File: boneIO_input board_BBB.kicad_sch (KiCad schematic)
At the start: 395 parts, among them J1 Screw_Terminal_01x08, J10 Screw_Terminal_01x04, J11 BeagleBone_Black_Header, J12 BeagleBone_Black_Header, J13 Conn_02x04_Odd_Even, J14 Screw_Terminal_01x08, J2 Screw_Terminal_01x08, J3 Screw_Terminal_01x08, J4 EXT_PSU, J5 Screw_Terminal_01x08, J6 Screw_Terminal_01x08, J7 Screw_Terminal_01x08, J8 Screw_Terminal_01x08, J9 Screw_Terminal_01x08, Q1 BSS84, SW1 SW_Push, SW2 SW_DIP_x04, U1 XL1509-5, U10 EL357N, U11 EL357N, U12 EL357N, U13 EL357N, U14 EL357N, U15 EL357N, U16 EL357N, U17 EL357N, U18 EL357N, U19 RT9013-33GB, U2 HLK-5D2405, U20 EL357N, U21 EL357N, U22 EL357N, U23 EL357N, U24 EL357N, U25 EL357N, U26 EL357N, U27 EL357N, U28 2N7002DW/BSS138PS, U29 EL357N, U3 EL357N, U30 EL357N, U31 EL357N, U32 EL357N, U33 EL357N, U34 EL357N, U35 EL357N, U36 EL357N, U37 DS1307Z+, U38 EL357N, U39 EL357N, U4 EL357N, U40 EL357N, U41 EL357N, U42 EL357N, U43 EL357N, U44 EL357N, U45 EL357N, U46 EL357N, U47 EL357N, U48 EL357N, U49 EL357N, U5 EL357N, U50 EL357N, U51 EL357N, U52 EL357N, U53 EL357N, U54 EL357N, U55 SN65HVD230, U56 RS485, U57 PCA9515, U58 PCA9515, U59 DS2482S-100+, U6 EL357N, U60 INA219AxD, U7 EL357N, U8 EL357N, U9 EL357N, Y1 32,788 MHz

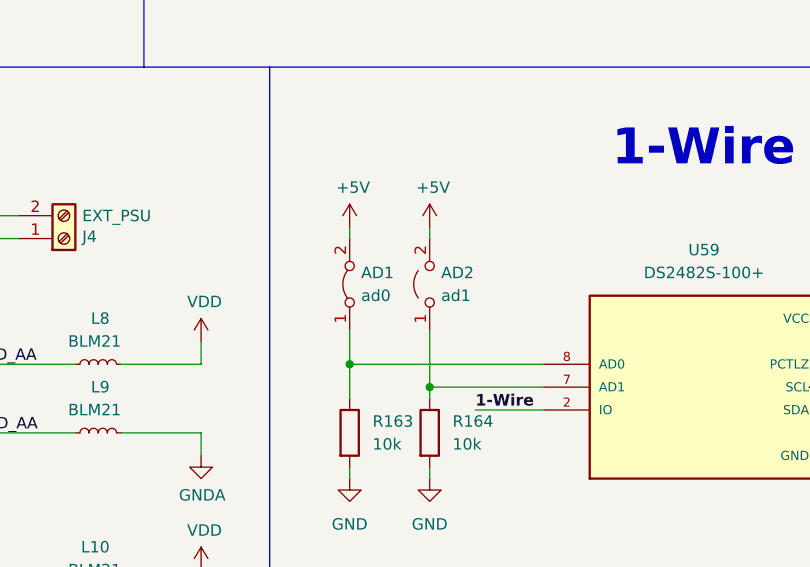
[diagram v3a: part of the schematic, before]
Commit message: input_board_v0.4
final version
descriptions added
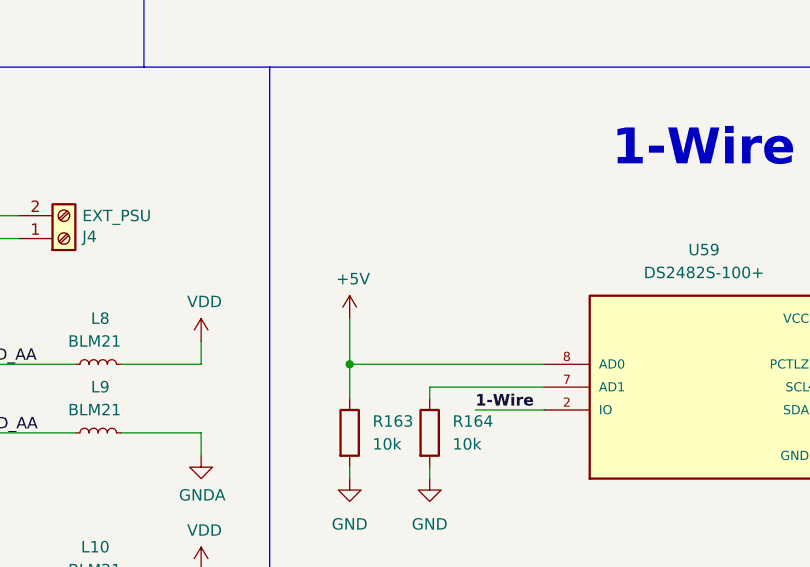
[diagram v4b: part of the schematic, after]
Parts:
- removed AD1: ad0, Jumper:SolderJumper-2_P1.3mm_Bridged2Bar_RoundedPad1.0x1.5mm, symbol Jumper:Jumper_2_Bridged
- removed AD2: ad1, Jumper:SolderJumper-2_P1.3mm_Open_RoundedPad1.0x1.5mm, symbol Jumper:Jumper_2_Open
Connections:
- net +5V: now also R163.1, U59.8 (AD0)
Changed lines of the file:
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@@
   (junction (at 402.59 459.74) (diameter 0) (color 0 0 0 0)
   )
-  (junction (at 652.78 410.21) (diameter 0) (color 0 0 0 0)
-  )
   (junction (at 170.18 229.87) (diameter 0) (color 0 0 0 0)
   )
@@
     (stroke (width 0) (type default) (color 0 0 0 0))
   )
-  (wire (pts (xy 652.78 392.43) (xy 652.78 393.7))
-    (stroke (width 0) (type default) (color 0 0 0 0))
-  )
   (wire (pts (xy 95.25 179.07) (xy 106.68 179.07))
     (stroke (width 0) (type default) (color 0 0 0 0))
@@
     (stroke (width 0) (type default) (color 0 0 0 0))
   )
-  (wire (pts (xy 643.89 403.86) (xy 643.89 407.67))
+  (wire (pts (xy 643.89 402.59) (xy 643.89 407.67))
     (stroke (width 0) (type default) (color 0 0 0 0))
   )
@@
     (stroke (width 0) (type default) (color 0 0 0 0))
   )
-  (wire (pts (xy 643.89 392.43) (xy 643.89 393.7))
-    (stroke (width 0) (type default) (color 0 0 0 0))
-  )
   (wire (pts (xy 567.69 347.98) (xy 570.23 347.98))
     (stroke (width 0) (type default) (color 0 0 0 0))
@@
     (stroke (width 0) (type default) (color 0 0 0 0))
   )
-  (wire (pts (xy 652.78 403.86) (xy 652.78 410.21))
-    (stroke (width 0) (type default) (color 0 0 0 0))
-  )
   (wire (pts (xy 247.65 312.42) (xy 254 312.42))
     (stroke (width 0) (type default) (color 0 0 0 0))
@@
     (pin "1")
   )
-  (symbol (lib_id "Jumper:Jumper_2_Bridged") (at 643.89 398.78 90) (unit 1)
-    (in_bom yes) (on_board yes) (fields_autoplaced)
-    (property "Reference" "AD1" (id 0) (at 645.16 397.5099 90)
-      (effects (font (size 1.27 1.27)) (justify right))
-    )
-    (property "Value" "ad0" (id 1) (at 645.16 400.0499 90)
-      (effects (font (size 1.27 1.27)) (justify right))
-    )
-    (property "Footprint" "Jumper:SolderJumper-2_P1.3mm_Bridged2Bar_RoundedPad1.0x1.5mm" (id 2) (at 643.89 398.78 0)
-      (effects (font (size 1.27 1.27)) hide)
-    )
-    (property "Datasheet" "~" (id 3) (at 643.89 398.78 0)
-      (effects (font (size 1.27 1.27)) hide)
-    )
-    (pin "1")
-    (pin "2")
-  )
   (symbol (lib_id "Device:R") (at 486.41 373.38 180) (unit 1)
     (in_bom yes) (on_board yes)
@@
     (pin "2")
   )
-  (symbol (lib_id "power:+5V") (at 652.78 392.43 0) (unit 1)
-    (in_bom yes) (on_board yes)
-    (property "Reference" "#PWR0333" (id 0) (at 652.78 396.24 0)
-      (effects (font (size 1.27 1.27)) hide)
-    )
-    (property "Value" "+5V" (id 1) (at 653.161 388.0358 0))
-    (property "Footprint" "" (id 2) (at 652.78 392.43 0)
-      (effects (font (size 1.27 1.27)) hide)
-    )
-    (property "Datasheet" "" (id 3) (at 652.78 392.43 0)
-      (effects (font (size 1.27 1.27)) hide)
-    )
-    (pin "1")
-  )
   (symbol (lib_id "Device:L_Small") (at 537.21 419.1 270) (unit 1)
     (in_bom yes) (on_board yes)
@@
     (pin "1")
   )
-  (symbol (lib_id "power:+5V") (at 643.89 392.43 0) (unit 1)
+  (symbol (lib_id "power:+5V") (at 643.89 402.59 0) (unit 1)
     (in_bom yes) (on_board yes)
-    (property "Reference" "#PWR0326" (id 0) (at 643.89 396.24 0)
+    (property "Reference" "#PWR0326" (id 0) (at 643.89 406.4 0)
       (effects (font (size 1.27 1.27)) hide)
     )
-    (property "Value" "+5V" (id 1) (at 644.271 388.0358 0))
-    (property "Footprint" "" (id 2) (at 643.89 392.43 0)
+    (property "Value" "+5V" (id 1) (at 644.271 398.1958 0))
+    (property "Footprint" "" (id 2) (at 643.89 402.59 0)
       (effects (font (size 1.27 1.27)) hide)
     )
-    (property "Datasheet" "" (id 3) (at 643.89 392.43 0)
+    (property "Datasheet" "" (id 3) (at 643.89 402.59 0)
       (effects (font (size 1.27 1.27)) hide)
     )
@@
     (pin "1")
   )
-  (symbol (lib_id "Jumper:Jumper_2_Open") (at 652.78 398.78 90) (unit 1)
-    (in_bom yes) (on_board yes) (fields_autoplaced)
-    (property "Reference" "AD2" (id 0) (at 654.05 397.5099 90)
-      (effects (font (size 1.27 1.27)) (justify right))
-    )
-    (property "Value" "ad1" (id 1) (at 654.05 400.0499 90)
-      (effects (font (size 1.27 1.27)) (justify right))
-    )
-    (property "Footprint" "Jumper:SolderJumper-2_P1.3mm_Open_RoundedPad1.0x1.5mm" (id 2) (at 652.78 398.78 0)
-      (effects (font (size 1.27 1.27)) hide)
-    )
-    (property "Datasheet" "~" (id 3) (at 652.78 398.78 0)
-      (effects (font (size 1.27 1.27)) hide)
-    )
-    (pin "1")
-    (pin "2")
-  )
   (symbol (lib_id "Device:LED_ALT") (at 486.41 266.7 90) (unit 1)
     (in_bom yes) (on_board yes)
@@
       (reference "#PWR0332") (unit 1) (value "GND") (footprint "")
     )
-    (path "/747e0037-5432-4d12-a50b-f417311ff954"
-      (reference "#PWR0333") (unit 1) (value "+5V") (footprint "")
-    )
     (path "/93c6fa48-78e3-448c-b7a0-b783a173c002"
       (reference "#PWR0334") (unit 1) (value "GND") (footprint "")
@@
       (reference "#PWR0370") (unit 1) (value "Earth") (footprint "")
     )
-    (path "/16d9ee91-9f7e-4305-88b4-ae4dabd60b80"
-      (reference "AD1") (unit 1) (value "ad0") (footprint "Jumper:SolderJumper-2_P1.3mm_Bridged2Bar_RoundedPad1.0x1.5mm")
-    )
-    (path "/a311dad9-240d-4934-809a-861307cc6006"
-      (reference "AD2") (unit 1) (value "ad1") (footprint "Jumper:SolderJumper-2_P1.3mm_Open_RoundedPad1.0x1.5mm")
-    )
     (path "/00000000-0000-0000-0000-000062d1d94e"

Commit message: input_board_v7.1
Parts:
- removed BT1: Battery, Battery:Battery_Panasonic_CR1220-VCN_Vertical_CircularHoles, symbol Device:Battery
- removed C20, C22: 1uF, Capacitor_SMD:C_0805_2012Metric, symbol Device:C
- removed C21: 460p, Capacitor_SMD:C_0603_1608Metric, symbol Device:C
- removed C40, C59, C61: 100n, Capacitor_SMD:C_0603_1608Metric, symbol Device:C
- removed D12, D15, D16, D17, D18, D19, D2, D22, D23, D24, D25, D26, D27, D28, D29, D3, D30, D31, D32, D33, D34, D35, D36, D37, D38, D39, D4, D40, D41, D42, D43, D44, D45, D46, D47, D48, D49, D5, D50, D53, D54, D55, D56, D6, D9: LED, LED_SMD:LED_0603_1608Metric, symbol Device:LED_ALT
- removed D51, D52: B5819W, Diode_SMD:D_SOD-123, symbol Device:D_ALT
- removed D57, D58: LED_GREEN, Capacitor_SMD:C_0805_2012Metric, symbol Device:LED
- removed D60: 5V6, Diode_SMD:D_MiniMELF, symbol Device:D_Zener_ALT
- removed D61: PESD5V0S2BT, Package_TO_SOT_SMD:SOT-23, symbol Diode:BAT54A
- removed J4: EXT_PSU, Connector_Phoenix_MSTB:PhoenixContact_MSTBA_2,5_2-G_1x02_P5.00mm_Horizontal, symbol Connector:Screw_Terminal_01x02
- removed L10, L11, L2, L3, L8, L9: BLM21, Inductor_SMD:L_0805_2012Metric, symbol Device:L_Small
- removed L5, L6, L7: BLM21_NC, Inductor_SMD:L_0805_2012Metric, symbol Device:L_Small
- removed Q1: BSS84, Package_TO_SOT_SMD:SOT-23, symbol Transistor_FET:BSS84
- removed R106, R130, R131, R146, R159, R51, R78: 680R, Resistor_SMD:R_0603_1608Metric, symbol Device:R
- removed R115: 10k, Resistor_SMD:R_0603_1608Metric, symbol Device:R
- removed R35: 100k, Resistor_SMD:R_0603_1608Metric, symbol Device:R
- removed R89, R90: 4.7k, Resistor_SMD:R_0603_1608Metric, symbol Device:R
- removed U19: RT9013-33GB, Package_TO_SOT_SMD:SOT-23-5, symbol Reference_Voltage:RT9013-33GB
- removed U2: HLK-5D2405, 3D_model:HLK5D2405, symbol Power_Management:HLK-5D2405
- removed U28: 2N7002DW/BSS138PS, Package_TO_SOT_SMD:SOT-363_SC-70-6, symbol Transistor_FET:2N7002DW
- removed U37: DS1307Z+, Package_SO:SOIC-8_3.9x4.9mm_P1.27mm, symbol Timer_RTC:DS1307Z+
- removed U56: RS485, rs485:RS485_moduleTTL, symbol RS485:RS485_module
- removed U57: PCA9515, Package_SO:TSSOP-8_3x3mm_P0.65mm, symbol Interface_Expansion:PCA9515
- removed U58: PCA9515, Package_SO:SO-8_3.9x4.9mm_P1.27mm, symbol Interface_Expansion:PCA9515
- removed U59: DS2482S-100+, Package_SO:SOP-8_3.9x4.9mm_P1.27mm, symbol DS2482S-100_:DS2482S-100+
- removed WIRE1: SPU, Jumper:SolderJumper-2_P1.3mm_Open_RoundedPad1.0x1.5mm, symbol Jumper:Jumper_2_Open
- removed Y1: 32,788 MHz, Crystal:Crystal_C26-LF_D2.1mm_L6.5mm_Horizontal, symbol Device:Crystal
- added C104, C105, C106, C107, C108, C109, C11, C110, C12, C13, C14, C15, C16, C17, C18, C29, C30, C31, C32, C33, C34, C35, C36, C37, C47, C48, C49, C51, C52, C53, C54, C55, C64, C65, C66, C67, C68, C69, C70, C71, C81, C82, C83, C84, C85, C86, C87, C88, C94, C95, C96, C97, C98: 100n, Capacitor_SMD:C_0603_1608Metric, symbol Device:C
- added C28, C38: 10uF, Capacitor_SMD:C_1206_3216Metric, symbol Device:C
- added D1: SMBJ24CA, Diode_SMD:D_SMB, symbol Diode:SM6T18A
- added D10: SMBJ5.0A, Diode_SMD:D_SMB, symbol Diode:SM6T18A
- added D11, D15: SMLVT3V3, Diode_SMD:D_SOD-323_HandSoldering, symbol Diode:B220
- added D12: SM712_SOT23, Package_TO_SOT_SMD:SOT-23, symbol Diode:SM712_SOT23
- added Q1: BC807, Package_TO_SOT_SMD:SOT-23, symbol Transistor_BJT:BC807
- added Q2: BSS138, Package_TO_SOT_SMD:SOT-23, symbol Transistor_FET:BSS138
- added R122, R123, R141, R155, R43, R70, R98: 680R, Resistor_SMD:R_0603_1608Metric, symbol Device:R
- added R162: 1k, Resistor_SMD:R_1206_3216Metric, symbol Device:R
- added R168, R172: 4.7k, Resistor_SMD:R_0603_1608Metric, symbol Device:R
- added R171: 120R, Resistor_SMD:R_0805_2012Metric, symbol ESP32-EVB_Rev_I:R
- added R173, R178, R179, R180: 0k, Resistor_SMD:R_0603_1608Metric, symbol Device:R
- added R176, R177: 1k, Resistor_SMD:R_0603_1608Metric, symbol Device:R
- added RS485_T1: Opened, Jumper:SolderJumper-2_P1.3mm_Open_RoundedPad1.0x1.5mm, symbol ESP32-EVB_Rev_I:SJ
- added U1: ADuM1250, Package_SO:SOIC-8_3.9x4.9mm_P1.27mm, symbol Isolator:ADuM1250
- added U19: AMS1117-3.3, Package_TO_SOT_SMD:SOT-223-3_TabPin2, symbol Regulator_Linear:AMS1117-3.3
- added U56: MAX485E, Package_SO:SOIC-8_3.9x4.9mm_P1.27mm, symbol Interface_UART:MAX485E
- D13, D14, D7, D8: value LED -> LED_RED
- D4: renamed from D11; footprint LED_SMD:LED_0805_2012Metric -> LED_SMD:LED_0603_1608Metric
- D5: renamed from D20; footprint LED_SMD:LED_0805_2012Metric -> LED_SMD:LED_0603_1608Metric
- F1: value Fuse_2A -> Fuse 2A; footprint Fuse:Fuse_2512_6332Metric -> Fuse:Fuse_1812_4532Metric; JLCPCB C136367 -> (none)
- L4: value BLM21_NC -> BLM21PG121SN1D
- R121: renamed from R123; value 1.5k -> 10k
- R160: renamed from R161; value 330R -> 1k
- R161: renamed from R162; value 330R -> 1k
- R163: value 10k -> 1k; footprint Resistor_SMD:R_0603_1608Metric -> Resistor_SMD:R_1206_3216Metric; JLCPCB (none) -> C101062
- R164: value 10k -> 4.7k
- R165, R166: value 10k -> 4.7k; JLCPCB C269704 -> (none)
- R167: value 50R -> 4.7k; JLCPCB (none) -> C269704
- R169: value 4.7k -> 0k; footprint Resistor_SMD:R_0603_1608Metric -> Resistor_SMD:R_0805_2012Metric
- R170: value 0R -> 0k_NC
- R34: renamed from R26; value 330R -> 1k
- R51: renamed from R52; value 330R -> 1k
- RV1: footprint Varistor:RV_Disc_D7mm_W3.5mm_P5mm -> Resistor_THT:R_Axial_DIN0204_L3.6mm_D1.6mm_P5.08mm_Vertical
- SW2: footprint Button_Switch_SMD:SW_DIP_SPSTx04_Slide_Omron_A6S-410x_W8.9mm_P2.54mm -> Button_Switch_THT:SW_DIP_SPSTx04_Piano_10.8x11.72mm_W7.62mm_P2.54mm
- U11, U12, U13, U14, U15, U16, U17, U18, U20, U21, U22, U23, U24, U25, U26, U27, U29, U30, U31, U32, U33, U34, U35, U36, U46, U47, U48, U49, U50, U51, U52, U53, U54: value EL357N -> EL354N
- U2: renamed from U3; value EL357N -> EL354N
- U3: renamed from U4; value EL357N -> EL354N
- U37: renamed from U38; value EL357N -> EL354N
- U38: renamed from U39; value EL357N -> EL354N
- U39: renamed from U40; value EL357N -> EL354N
- U4: renamed from U5; value EL357N -> EL354N
- U40: renamed from U41; value EL357N -> EL354N
- U41: renamed from U42; value EL357N -> EL354N
- U42: renamed from U43; value EL357N -> EL354N
- U43: renamed from U44; value EL357N -> EL354N
- U44: renamed from U45; value EL357N -> EL354N
- U5: renamed from U6; value EL357N -> EL354N
- U6: renamed from U7; value EL357N -> EL354N
- U7: renamed from U8; value EL357N -> EL354N
- U8: renamed from U9; value EL357N -> EL354N
- U9: renamed from U10; value EL357N -> EL354N
- renumbered C2 to C1, C55 to C100, C56 to C101, C57 to C102, C58 to C103, C60 to C111, C62 to C112, C11 to C19, C3 to C2, C12 to C20, C13 to C21, C14 to C22, C15 to C23, C16 to C24, C17 to C25, C18 to C26, C19 to C27, C4 to C3, C23 to C39, C5 to C4, C24 to C40, C25 to C41, C26 to C42, C27 to C43, C28 to C44, C29 to C45, C30 to C46, C6 to C5, C31 to C50, C32 to C56, C33 to C57, C34 to C58, C35 to C59, C7 to C6, C36 to C60, C37 to C61, C38 to C62, C39 to C63, C8 to C7, C41 to C73, C42 to C74, C43 to C75, C44 to C76, C45 to C77, C46 to C78, C47 to C79, C9 to C8, C48 to C80, C49 to C89, C1 to C9, C50 to C90, C51 to C91, C52 to C92, C53 to C93, C54 to C99, D1 to D2, D10 to D3, D21 to D6, D59 to D9, J9 to J10, J10 to J11, J13 to J12, J14 to J13, J5 to J4, J6 to J5, J11 to J6, J12 to J9, L1 to L3, R11 to R10, R107 to R106, R108 to R107, R109 to R108, R110 to R109, R12 to R11, R111 to R110, R112 to R111, R113 to R112, R114 to R113, R116 to R114, R117 to R115, R118 to R116, R119 to R117, R120 to R118, R121 to R119, R13 to R12, R122 to R120, R14 to R13, R132 to R131, R133 to R132, R134 to R133, R135 to R134, R136 to R135, R137 to R136, R138 to R137, R139 to R138, R140 to R139, R15 to R14, R141 to R140, R147 to R146, R148 to R147, R149 to R148, R150 to R149, R16 to R15, R151 to R150, R152 to R151, R153 to R152, R154 to R153, R155 to R154, R160 to R159, R17 to R16, R9 to R17, R168 to R174, R171 to R175, R27 to R26, R28 to R27, R29 to R28, R30 to R29, R31 to R30, R32 to R31, R33 to R32, R34 to R33, R36 to R35, R37 to R36, R38 to R37, R39 to R38, R40 to R39, R41 to R40, R42 to R41, R43 to R42, R53 to R52, R54 to R53, R55 to R54, R56 to R55, R57 to R56, R58 to R57, R59 to R58, R60 to R59, R61 to R60, R63 to R61, R64 to R62, R65 to R63, R66 to R64, R67 to R65, R68 to R66, R69 to R67, R70 to R68, R62 to R69, R79 to R78, R81 to R79, R82 to R80, R83 to R81, R84 to R82, R85 to R83, R86 to R84, R87 to R85, R88 to R86, R80 to R87, R91 to R89, R10 to R9, R92 to R90, R93 to R91, R94 to R92, R95 to R93, R96 to R94, R97 to R95, R98 to R96, U1 to U10, U60 to U58
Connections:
- net SDA_5V is gone; now on net SDA: R87.2
- net +24V: now also SW2.5, SW2.7
- net +3V3: now also D13.2 (A), D14.2 (A), D7.2 (A), D8.2 (A), R166.1, R167.2, R87.1, C109.1, C110.1, C38.1, D11.1 (K), Q1.2 (E), Q2.1 (G), R180.2, U1.1 (VDD1), U19.2 (VO), U56.8 (VCC); no longer J11.4 (Pin_4), R100.2, R101.2, R102.2, R103.2, R104.2, R105.2, R124.2, R125.2, R126.2, R127.2, R128.2, R129.2, R142.2, R143.2, R144.2, R145.2, R156.2, R157.2, R158.2, R18.2, R19.2, R20.2, R21.2, R22.2, R23.2, R24.2, R25.2, R44.2, R45.2, R46.2, R47.2, R48.2, R49.2, R50.2, R71.2, R72.2, R73.2, R74.2, R75.2, R76.2, R77.2, R99.2
- net +5V: now also C28.1, C29.1, R172.2, U19.3 (VI); no longer R163.1, R165.1, R166.1, R167.2, R169.2, R87.1
- net 1-Wire: now also R170.1, Q2.3 (D), R172.1; no longer R170.2
- net 1-Wire_OUT: now also R167.1, R170.2, Q2.2 (S); no longer R169.1, R170.1
- net A+_OUT: now also R166.2, D12.2 (A2), R171.2, U56.6 (A)
- net B-_OUT: now also D12.1 (A1), R168.1, RS485_T1.2, U56.7 (B)
- net GND: now also C10.2, C19.2, C9.2, D3.2 (A), D4.1 (K), J12.2 (Pin_2), J12.4 (Pin_4), L4.1, R165.2, R169.2, R17.2, SW2.6, SW2.8, U10.5 (GND), U10.6 (GND), U10.7 (GND), U10.8 (GND), C104.2, C105.2, C106.2, C107.2, C108.2, C109.2, C11.2, C110.2, C12.2, C13.2, C14.2, C15.2, C16.2, C17.2, C18.2, C28.2, C29.2, C30.2, C31.2, C32.2, C33.2, C34.2, C35.2, C36.2, C37.2, C38.2, C47.2, C48.2, C49.2, C51.2, C52.2, C53.2, C54.2, C55.2, C64.2, C65.2, C66.2, C67.2, C68.2, C69.2, C70.2, C71.2, C81.2, C82.2, C83.2, C84.2, C85.2, C86.2, C87.2, C88.2, C94.2, C95.2, C96.2, C97.2, C98.2, D10.2 (A2), D15.2 (A), R168.2, R179.2, U1.4 (GND1), U19.1 (GND), U56.5 (GND); no longer J1.8 (Pin_8), J11.1 (Pin_1), R163.2, R164.2
- net GND1: no longer SW2.7
- net GND2: no longer J13.8 (Pin_8)
- net GNDA: now also SW2.2, R162.2
- net GND_ADC: now also D11.2 (A)
- net I2C_SCL_OUT: now also R178.1, U1.6 (SCL2); no longer R166.2
- net I2C_SDA_OUT: now also R173.1, U1.7 (SDA2); no longer R165.2
- net P8.07: now also R123.2; no longer R115.1, U38.4
- net P8.08: now also R122.2; no longer R114.1, U37.4
- net P8.09: now also R98.2; no longer R96.1, U36.4
- net P8.10: now also R105.2; no longer R95.1, U35.4
- net P8.11: now also R104.2; no longer R94.1, U34.4
- net P8.12: now also R103.2; no longer R93.1, U33.4
- net P8.13: now also R102.2; no longer R92.1, U32.4
- net P8.14: now also R101.2; no longer R91.1, U31.4
- net P8.15: now also R100.2; no longer R90.1, U30.4
- net P8.16: now also R99.2; no longer R89.1, U29.4
- net P8.17: now also R72.2; no longer R63.1, U22.4
- net P8.18: now also R71.2; no longer R62.1, U21.4
- net P8.19: now also R70.2; no longer R61.1, U20.4
- net P8.26: now also R77.2; no longer R68.1, U27.4
- net P8.27: now also R76.2; no longer R67.1, U26.4
- net P8.28: now also R75.2; no longer R66.1, U25.4
- net P8.29: now also R74.2; no longer R65.1, U24.4
- net P8.30: now also R73.2; no longer R64.1, U23.4
- net P8.31: now also R50.2; no longer R42.1, U18.4
- net P8.32: now also R49.2; no longer R41.1, U17.4
- net P8.33: now also R48.2; no longer R40.1, U16.4
- net P8.34: now also R47.2; no longer R39.1, U15.4
- net P8.35: now also R46.2; no longer R38.1, U14.4
- net P8.36: now also R45.2; no longer D14.1 (K), R37.1, U13.4
- net P8.37: now also R44.2; no longer D13.1 (K), R36.1, U12.4
- net P8.38: now also R43.2; no longer R35.1, U11.4
- net P8.39: now also R23.2; no longer R16.1, U9.4
- net P8.40: now also R20.2; no longer D8.1 (K), R15.1, U8.4
- net P8.41: now also R19.2; no longer D7.1 (K), R14.1, U7.4
- net P8.42: now also R18.2; no longer R13.1, U6.4
- net P8.43: now also R22.2; no longer R12.1, U5.4
- net P8.44: now also R21.2; no longer R11.1, U4.4
- net P8.45: now also R25.2; no longer R10.1, U3.4
- net P8.46: now also R24.2; no longer R9.1, U2.4
- net P9.14: now also R124.2; no longer R116.1, U39.4
- net P9.15: now also R125.2; no longer R117.1, U40.4
- net P9.16: now also R127.2; no longer R118.1, U41.4
- net P9.17: now also R141.2; no longer R136.1, U46.4
- net P9.18: now also R142.2; no longer R137.1, U47.4
- net P9.21: now also R143.2; no longer R138.1, U48.4
- net P9.22: now also R144.2; no longer R139.1, U49.4
- net P9.23: now also R145.2; no longer R140.1, U50.4
- net P9.25: now also R128.2; no longer R119.1, U42.4
- net P9.27: now also R126.2; no longer R120.1, U43.4
- net P9.28: now also R129.2; no longer R121.1, U44.4
- net P9.29: now also R155.2; no longer R151.1, U51.4
- net P9.30: now also R156.2; no longer R152.1, U52.4
- net P9.31: now also R157.2; no longer R153.1, U53.4
- net P9.42: now also R158.2; no longer R154.1, U54.4
- net SCL: now also R178.2, U1.3 (SCL1)
- net SDA: now also R173.2, U1.2 (SDA1)
- net VDD: now also R163.2, SW2.4
- net VDD_ADC: now also D15.1 (K)
- net at C111.1, F2.1, J6.5 (Pin_5)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: now also D10.1 (A1)
- net at D2.2 (A), F1.1, RV1.1: now also D1.1 (A1)
- net at R156.1: now also R152.1, U52.4, C105.1
- net at R22.1: now also R12.1, U5.4, C15.1
- net at R127.1: now also R118.1, U41.4, C86.1
- net at R45.1: now also R37.1, U13.4, C32.1; no longer D13.2 (A)
- net at R48.1: now also R40.1, U16.4, C35.1
- net at R161.2: now also D8.1 (K)
- net at R143.1: now also R138.1, U48.4, C96.1
- net at R125.1: now also R117.1, U40.4, C84.1
- net at R129.1: now also R121.1, U44.4, C88.1
- net at R25.1: now also R10.1, U3.4, C18.1
- net at R104.1: now also R94.1, U34.4, C70.1
- net at R18.1: now also R13.1, U6.4, C11.1
- net at R158.1: now also R154.1, U54.4, C107.1
- net at R103.1: now also R93.1, U33.4, C69.1
- net at R145.1: now also R140.1, U50.4, C98.1
- net at R50.1: now also R42.1, U18.4, C37.1
- net at R144.1: now also R139.1, U49.4, C97.1
- net at R47.1: now also R39.1, U15.4, C34.1
- net at R20.1: now also R15.1, U8.4, C13.1
- net at R100.1: now also R90.1, U30.4, C66.1
- net at R49.1: now also R41.1, U17.4, C36.1
- net at R44.1: now also R36.1, U12.4, C31.1
- net at R72.1: now also R63.1, U22.4, C49.1
- net at R71.1: now also R62.1, U21.4, C48.1
- net at R19.1: now also R14.1, U7.4, C12.1
- net at R75.1: now also R66.1, U25.4, C53.1
- net at R23.1: now also R16.1, U9.4, C16.1; no longer D7.2 (A)
- net at R124.1: now also R116.1, U39.4, C83.1
- net at R101.1: now also R91.1, U31.4, C67.1
- net at R76.1: now also R67.1, U26.4, C54.1
- net at R142.1: now also R137.1, U47.4, C95.1
- net at R128.1: now also R119.1, U42.4, C87.1
- net at R126.1: now also R120.1, U43.4, C85.1
- net at R105.1: now also R95.1, U35.4, C71.1
- net at R74.1: now also R65.1, U24.4, C52.1
- net at R102.1: now also R92.1, U32.4, C68.1
- net at R21.1: now also R11.1, U4.4, C14.1
- net at R99.1: now also R89.1, U29.4, C65.1
- net at R24.1: now also R9.1, U2.4, C17.1; no longer D8.2 (A)
- net at R157.1: now also R153.1, U53.4, C106.1
- net at R164.1: now also Q1.1 (B)
- net at R73.1: now also R64.1, U23.4, C51.1
- net at R160.2: now also D7.1 (K)
- net at R46.1: now also R38.1, U14.4, C33.1; no longer D14.2 (A)
- net at R77.1: now also R68.1, U27.4, C55.1
- net CAN_RX renamed UART1_RX
- net CAN_TX renamed UART1_TX
- removed net Earth: C10.2, C19.2, C9.2, D3.2 (A), D4.1 (K), J12.2 (Pin_2), J12.4 (Pin_4), R17.2, RV1.2, SW2.8, U10.5 (GND), U10.6 (GND), U10.7 (GND), U10.8 (GND), VDD1.2 (Pin_2)
- net GND_AA: no longer names the net of SW2.1
- net GND_AA: now also R163.1; no longer SW2.2
- net RS485_RX renamed UART4_RX
- net UART4_RX: now also R177.1, U56.1 (RO)
- net RS485_TX renamed UART4_TX
- net UART4_TX: now also R164.2, R176.1, U56.4 (DI)
- removed net VDD_AA: L4.2, SW2.3, SW2.4
- new net: C30.1, R35.1, R43.1, U11.4
- new net: C81.1, R114.1, R122.1, U37.4
- new net: C64.1, R96.1, R98.1, U36.4
- new net: C47.1, R61.1, R70.1, U20.4
- new net: C104.1, R151.1, R155.1, U51.4
- new net: C94.1, R136.1, R141.1, U46.4
- new net: C82.1, R115.1, R123.1, U38.4
- new net: D13.1 (K), R176.2
- new net: D14.1 (K), R177.2
- new net: C108.1, Q1.3 (C), R165.1, U56.2 (~{RE}), U56.3 (DE)
- new net: R162.1, SW2.3
- new net: R171.1, RS485_T1.1
- new net GNDS: J11.1 (Pin_1), R179.1, U1.5 (GND2)
- new net GND_RS485: D12.3 (common), J13.8 (Pin_8), L4.2
- new net VDDF: J11.4 (Pin_4), R180.1, U1.8 (VDD2)
- new net VSS: D1.2 (A2), R169.1, RV1.2, VDD1.2 (Pin_2)
- no-connect marks 15 -> 16
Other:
- note added: "1-WIRE"
- note added: "AUTO PSU Switch"
- note added: "Input Board v0.7 BBB"
- note removed: "1-Wire"
- note removed: "C22 tylko w przypadku montażu MIC5219-3.3"
- note removed: "Clock RTC"
- note removed: "I2C"
- note removed: "Input Board v0.5 BBB"
- note removed: "Manual PSU Switch"
- moved on the sheet: ANVDD1, C1, C10, C100, C101, C102, C103, C111, C112, C19, C2, C20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
